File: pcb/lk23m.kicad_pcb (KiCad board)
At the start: 2 copper layers, 76.2 x 119.1 mm, 59 parts, among them J1 Conn_01x02, SW1 RotaryEncoder_Switch_MP, SW10 SW_Push, SW11 SW_Push, SW12 SW_Push, SW13 SW_Push, SW14 SW_Push, SW15 SW_Push, SW16 SW_Push, SW17 SW_Push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

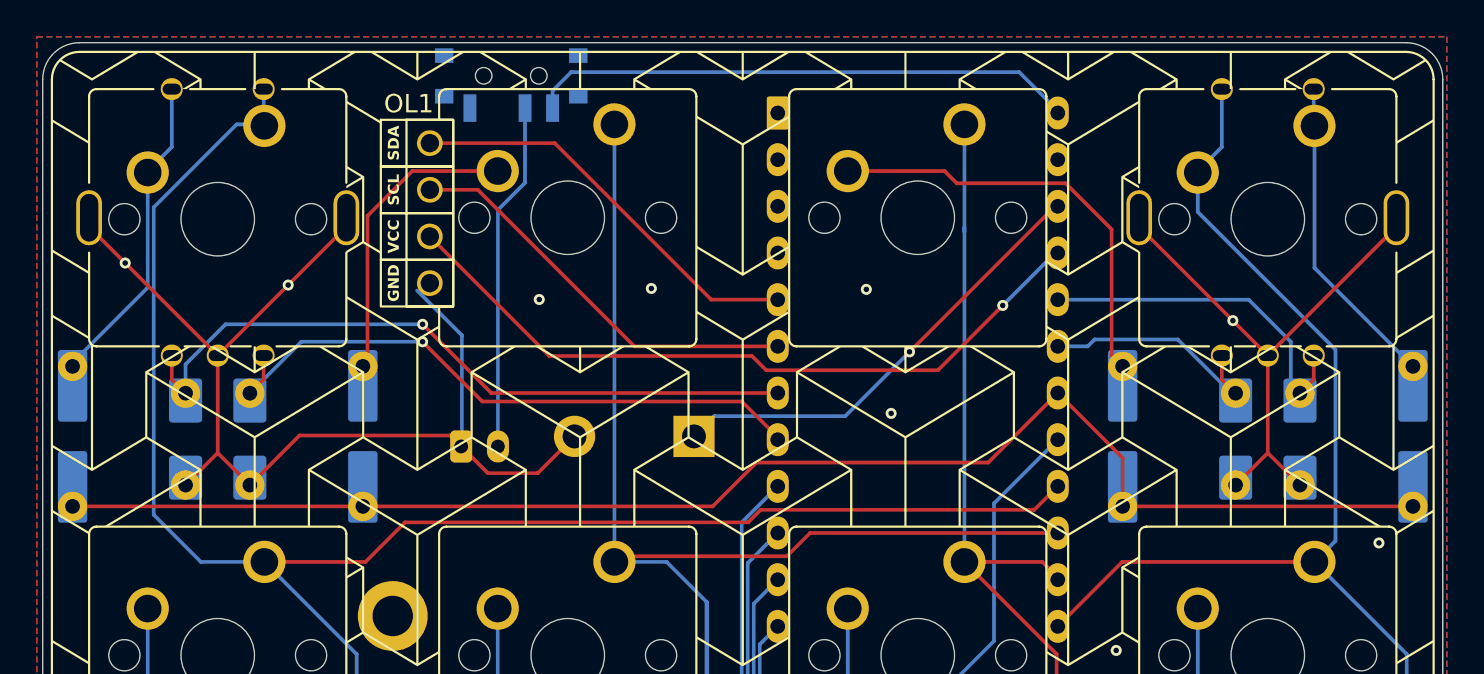
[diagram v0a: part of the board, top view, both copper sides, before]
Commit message: Model should be done, we should just look at exporting keyboard.pretty as a library
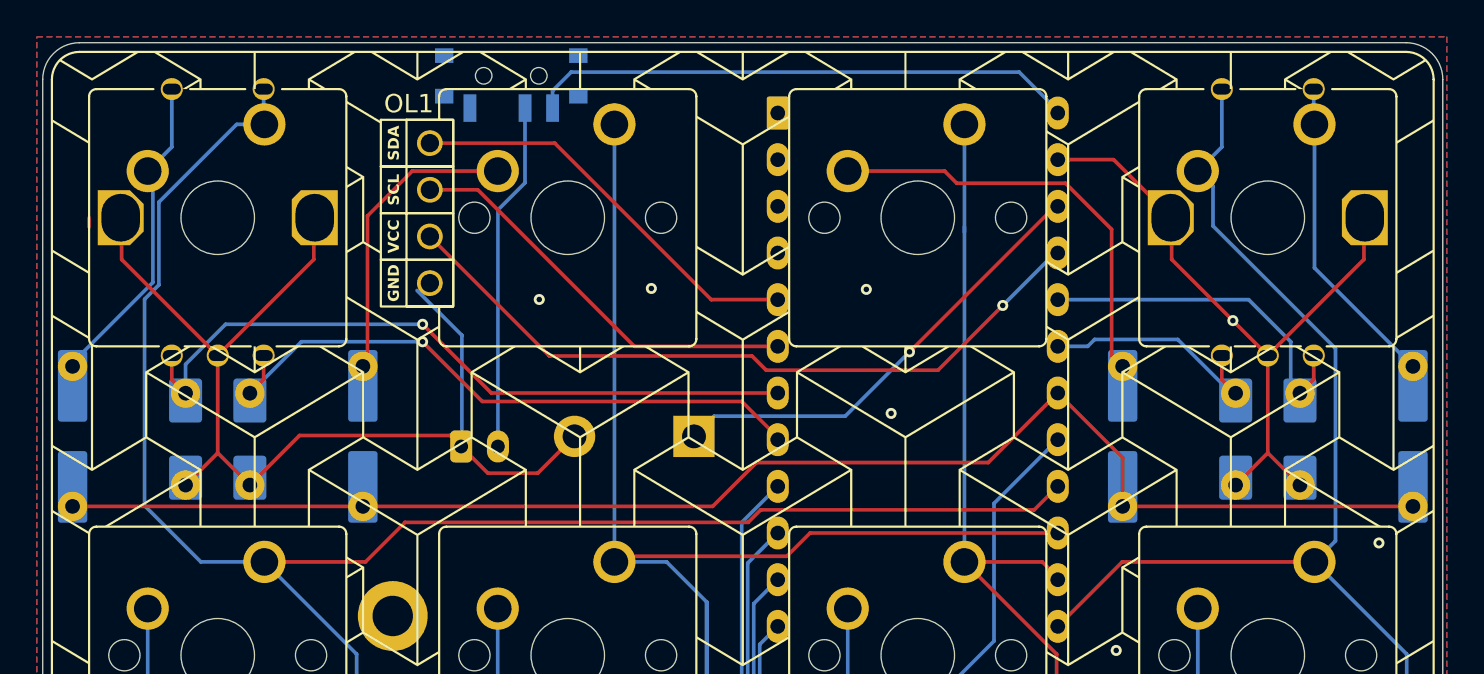
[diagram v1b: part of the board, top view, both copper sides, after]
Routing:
- net GND: track 92.1 -> 97.1 mm, vias 14 -> 12
- net E2S2: track 140.5 -> 139.5 mm

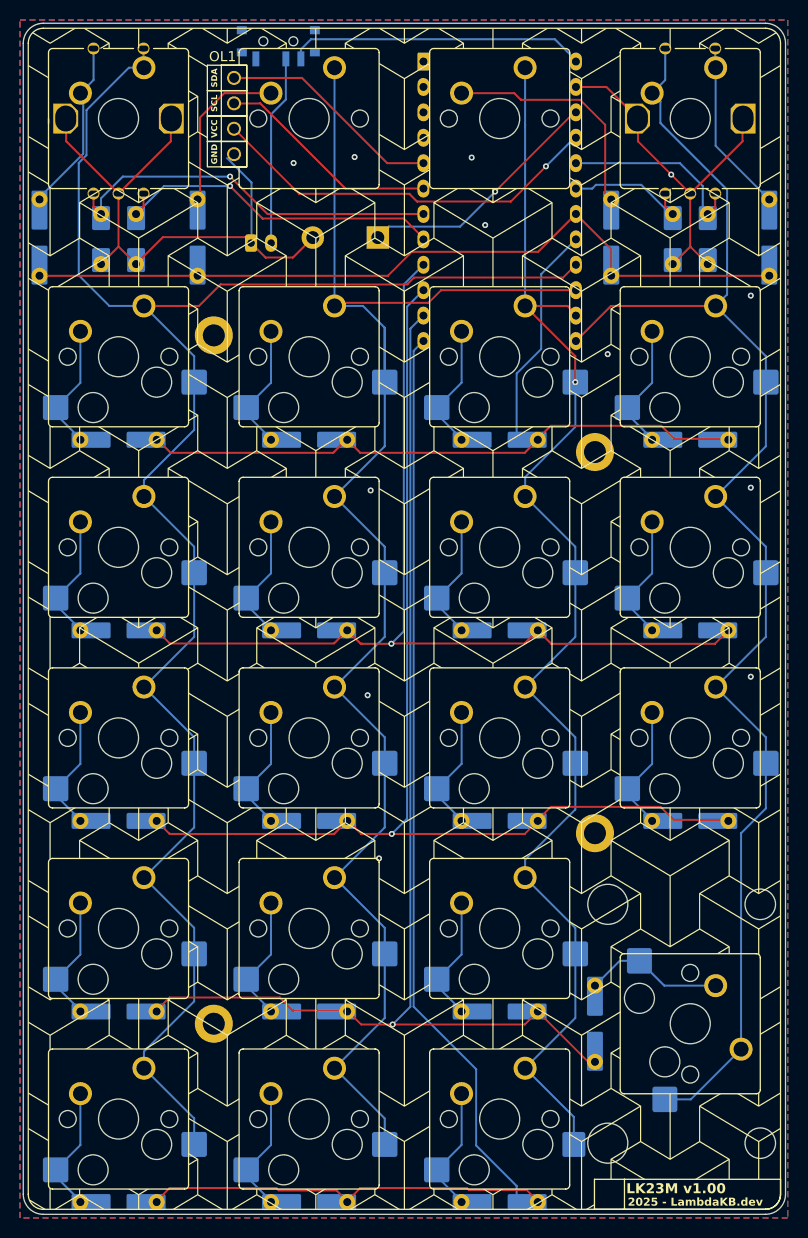
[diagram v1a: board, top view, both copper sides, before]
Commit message: Migrate to using symbols and footprints from gtihub.com/lambdakb/kicad-lkbd
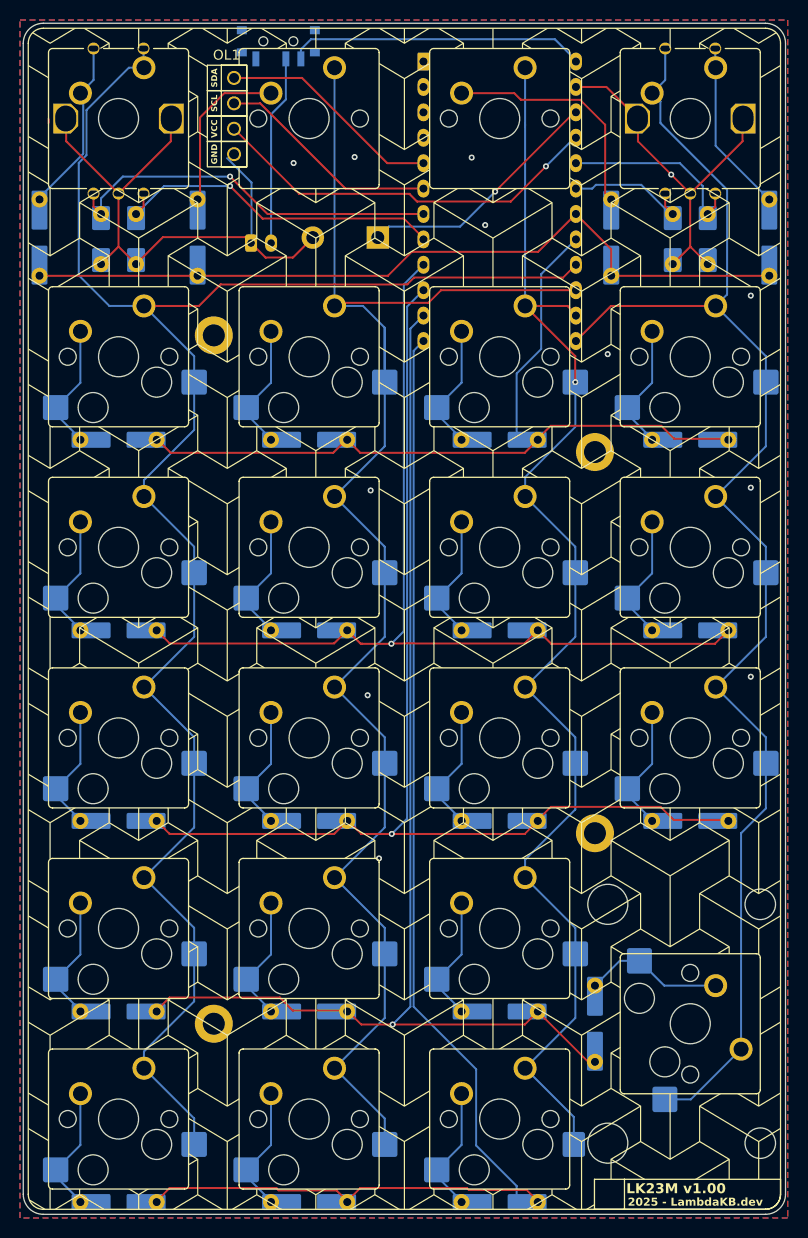
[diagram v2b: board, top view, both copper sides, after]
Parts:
- C1, C2, C3, C4: footprint keyboard:Capacitor_SMD+THT_1206_5.0x2.5mm_P5.00mm -> LKBD_Common:Capacitor_SMD+THT_1206_5.0x2.5mm_P5.00mm
- D1, D10, D11, D12, D13, D14, D15, D16, D17, D18, D19, D2, D20, D21, D22, D23, D3, D4, D5, D6, D7, D8, D9: footprint keyboard:Diode_SMD+THT_SOD123_DO35_P7.62mm -> LKBD_Common:Diode_SMD+THT_SOD123_DO35_P7.62mm
- OL1: footprint keyboard:OLED_SSD1306_128x32_0.91inch_I2C_btmSilk -> LKBD_OLED:OLED_SSD1306_128x32_0.91inch_I2C_btmSilk
- SW1, SW4: footprint keyboard:SW_MX_EC11_THT_sqSilk -> LKBD_KeySwitch:SW_MX_EC11_THT_sqSilk
- SW10, SW11, SW12, SW13, SW14, SW15, SW16, SW17, SW18, SW19, SW20, SW21, SW22, SW5, SW6, SW7, SW8, SW9: footprint keyboard:SW_MX_HotSwap_THT_sqSilk -> LKBD_KeySwitch:SW_MX_HotSwap_THT_sqSilk
- SW2, SW3: footprint keyboard:SW_MX_THT_sqSilk -> LKBD_KeySwitch:SW_MX_THT_sqSilk
- SW23: footprint keyboard:SW_MX_2U_HotSwap_THT_sqSilk -> LKBD_KeySwitch:SW_MX_2U_HotSwap_THT_sqSilk
- U1: value ProMicro -> ProMicro_RP2040; footprint keyboard:MCU_KB2040_DIP-24_Socket_Reverse -> LKBD_MCU:MCU_KB2040_DIP-24_Socket_Reverse

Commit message: Fix SMD footprint position + add kibot setup
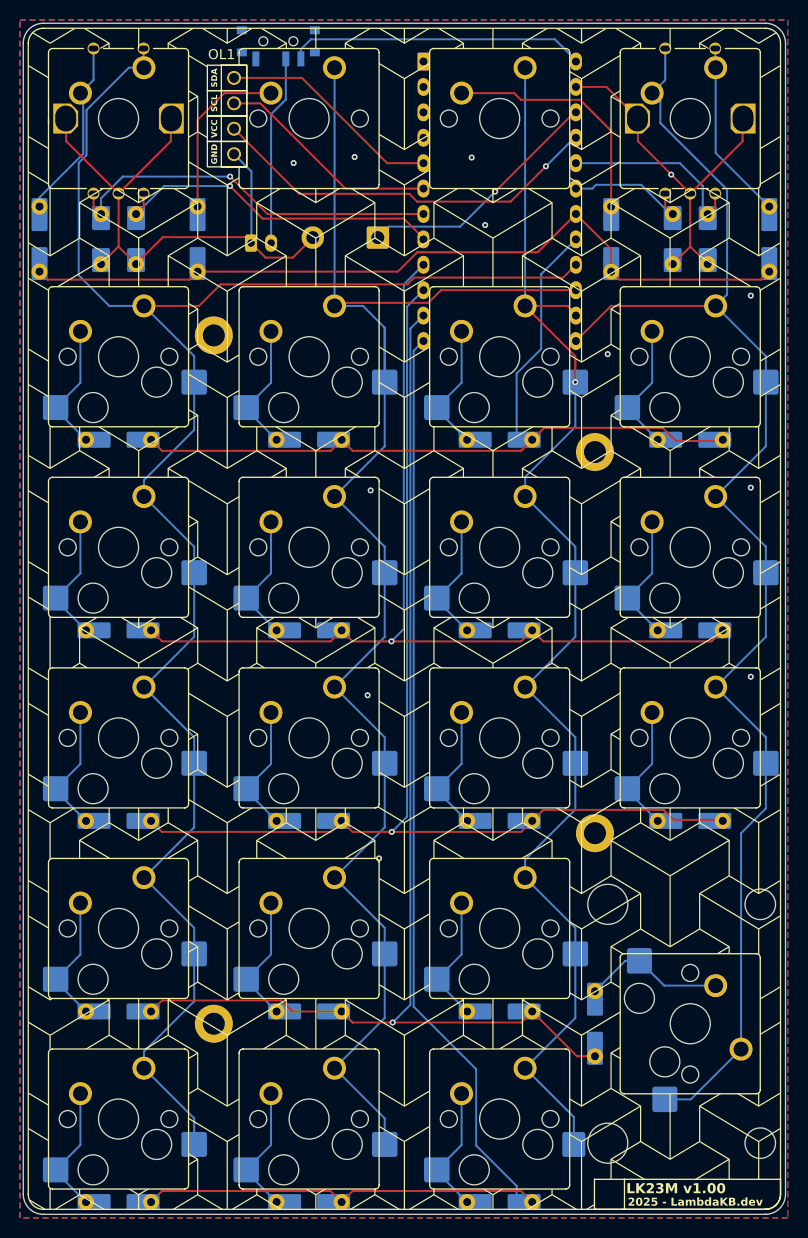
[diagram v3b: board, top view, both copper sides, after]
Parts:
- D1, D10, D11, D12, D13, D14, D15, D16, D17, D18, D19, D2, D20, D21, D22, D23, D3, D4, D5, D6, D7, D8, D9: footprint LKBD_Common:Diode_SMD+THT_SOD123_DO35_P7.62mm -> LKBD_Common:Diode_SMD+THT_SOD123_DO35_P6.5mm
- SW10, SW11, SW12, SW13, SW14, SW15, SW16, SW17, SW18, SW19, SW20, SW21, SW22, SW23, SW5, SW6, SW7, SW8, SW9: moved to B.Cu
- SW24: footprint Button_Switch_THT:SW_PUSH_1P1T_6x3.5mm_H4.3_APEM_MJTP1243 -> LKBD_Common:SW_PUSH_1P1T_6x3.5mm
- moved D1 0.15 mm to (30.2, 50.1)
- moved D2 0.15 mm to (46.0, 50.1)
- moved D3 0.15 mm to (87.3, 50.1)
- moved D4 0.15 mm to (103.2, 50.1)
- turned SW10 to 180 degrees
- turned SW11 to 180 degrees
- turned SW12 to 180 degrees
- turned SW13 to 180 degrees
- turned SW14 to 180 degrees
- turned SW15 to 180 degrees
- turned SW16 to 180 degrees
- turned SW17 to 180 degrees
- turned SW18 to 180 degrees
- turned SW19 to 180 degrees
- turned SW20 to 180 degrees
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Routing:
- net row0: track 79.6 -> 80.8 mm
- net Net-(D22-A): track 12.8 -> 13.8 mm
- net Net-(D20-A): track 12.8 -> 13.8 mm
- net Net-(D15-A): track 12.8 -> 13.8 mm
- net Net-(D12-A): track 12.8 -> 13.8 mm
- net Net-(D9-A): track 12.8 -> 13.8 mm
- net Net-(D21-A): track 12.8 -> 13.8 mm
- net Net-(D16-A): track 12.8 -> 13.8 mm
- net Net-(D13-A): track 12.8 -> 13.8 mm
- net Net-(D11-A): track 12.8 -> 13.8 mm
- net Net-(D14-A): track 12.8 -> 13.8 mm
- net Net-(D10-A): track 12.8 -> 13.8 mm
- net Net-(D17-A): track 12.8 -> 13.8 mm
- net Net-(D19-A): track 12.8 -> 13.8 mm
- net Net-(D18-A): track 12.8 -> 13.8 mm
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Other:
- board text added: "+"
- board text added: "-"
